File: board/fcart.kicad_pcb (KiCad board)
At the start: 2 copper layers, 100 x 62.7 mm, 96 parts, among them J1 USB_C_16P, J2 DM3D-SF, J3 JTAG, J4 SWD, J5 Famicom_cartridge, SW1 PTS647SM70, U1 USBLC6-2SC6, U10 W9864G6KH-6, U2 TLV76133DCY, U3 TPS2116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

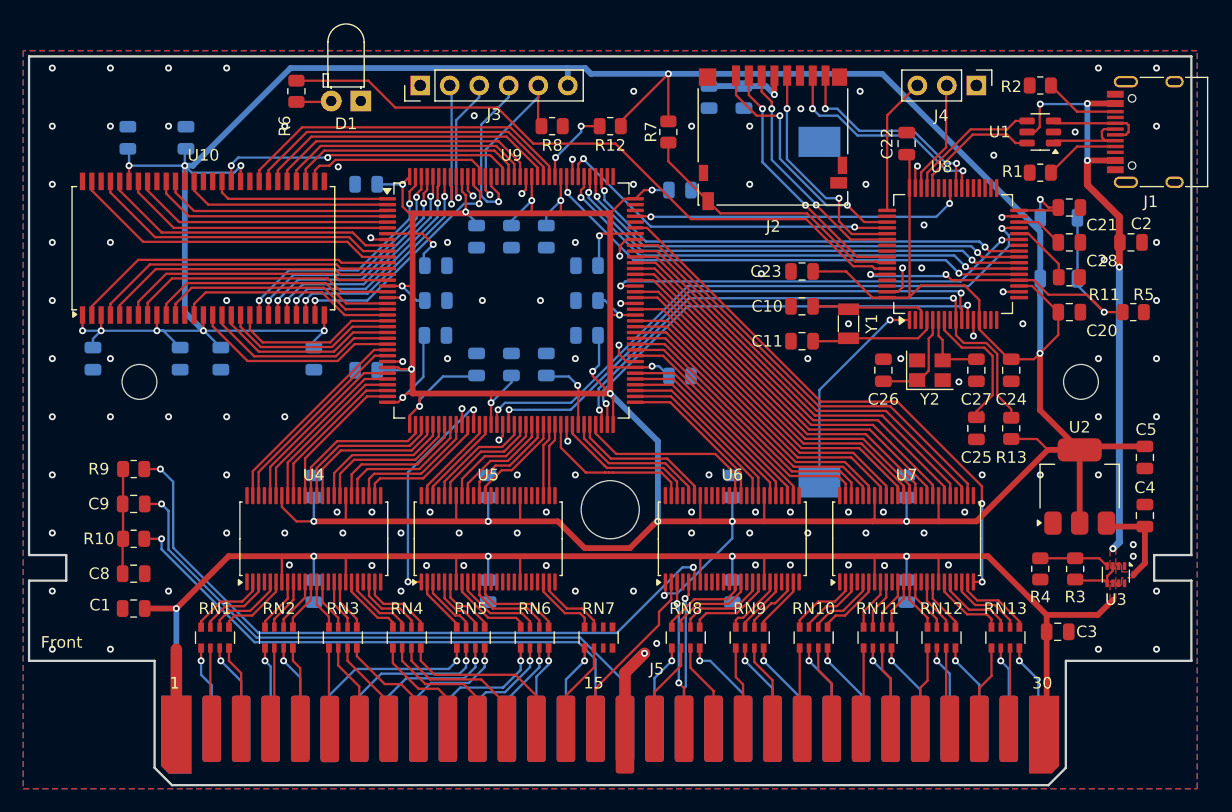
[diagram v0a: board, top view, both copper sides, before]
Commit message: open edge connectors
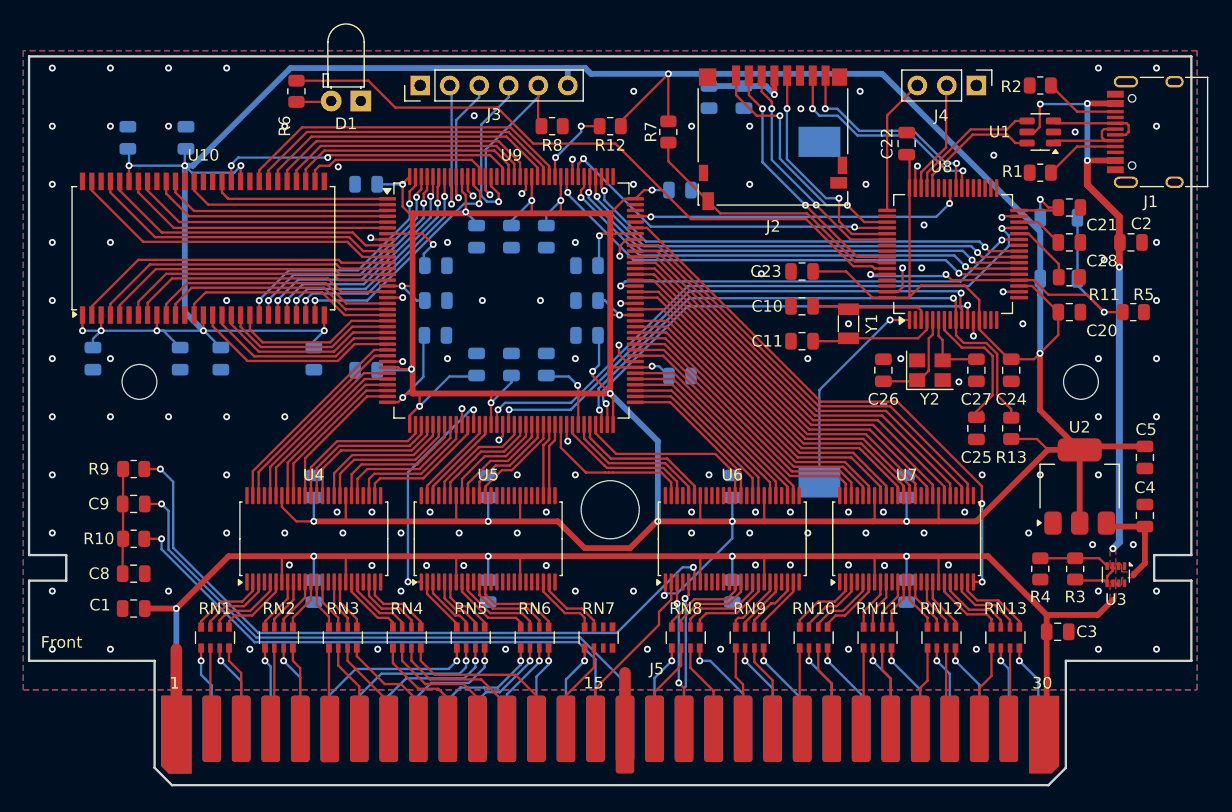
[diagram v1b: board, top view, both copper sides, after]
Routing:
- net GND: track 44.9 -> 42.6 mm, vias 127 -> 134

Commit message: added restrictive zones
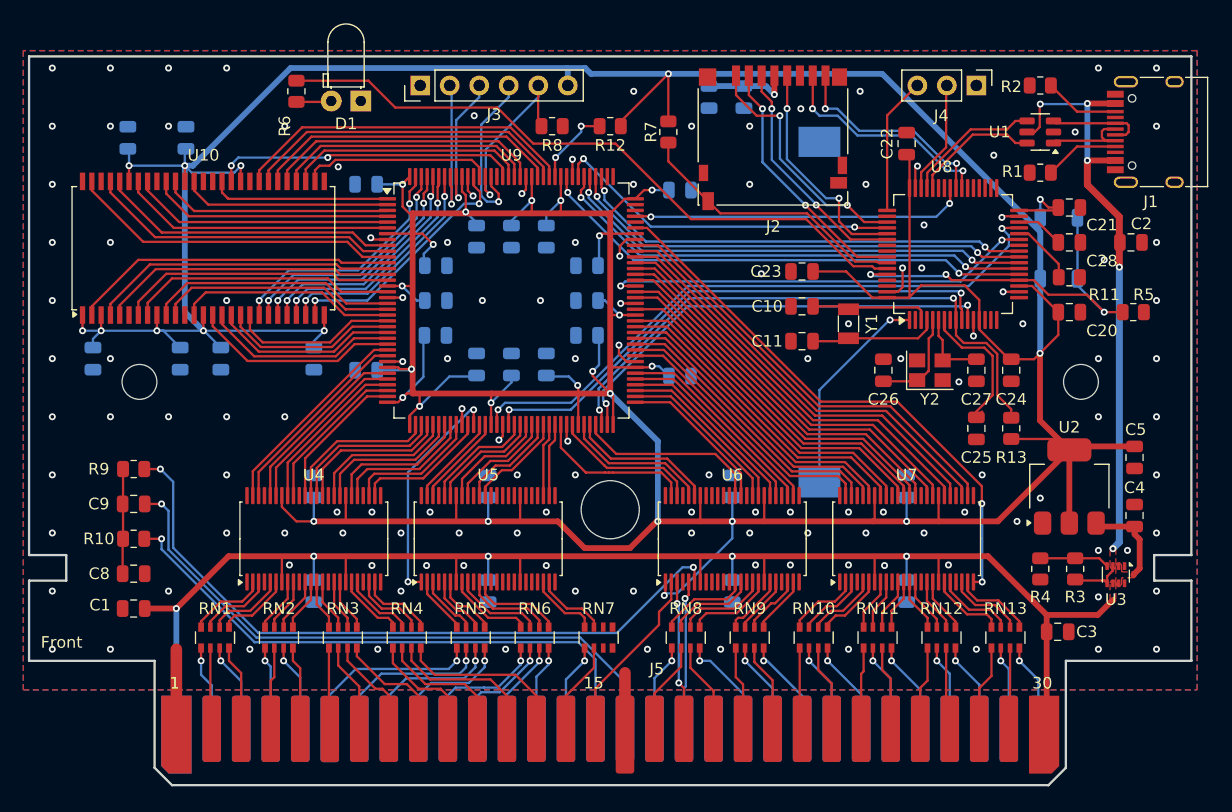
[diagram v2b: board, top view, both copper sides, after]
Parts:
- moved C4 0.89 mm to (198.1, 108.5)
- moved C5 0.89 mm to (198.1, 103.5)
- moved U2 0.89 mm to (192.5, 106.0)
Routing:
- net +3V3: track 546.3 -> 546.9 mm
- net GND: vias 134 -> 135
